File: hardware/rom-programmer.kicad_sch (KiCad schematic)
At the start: 4 parts, among them U1 74HC595, U2 74HC595, U3 28C256

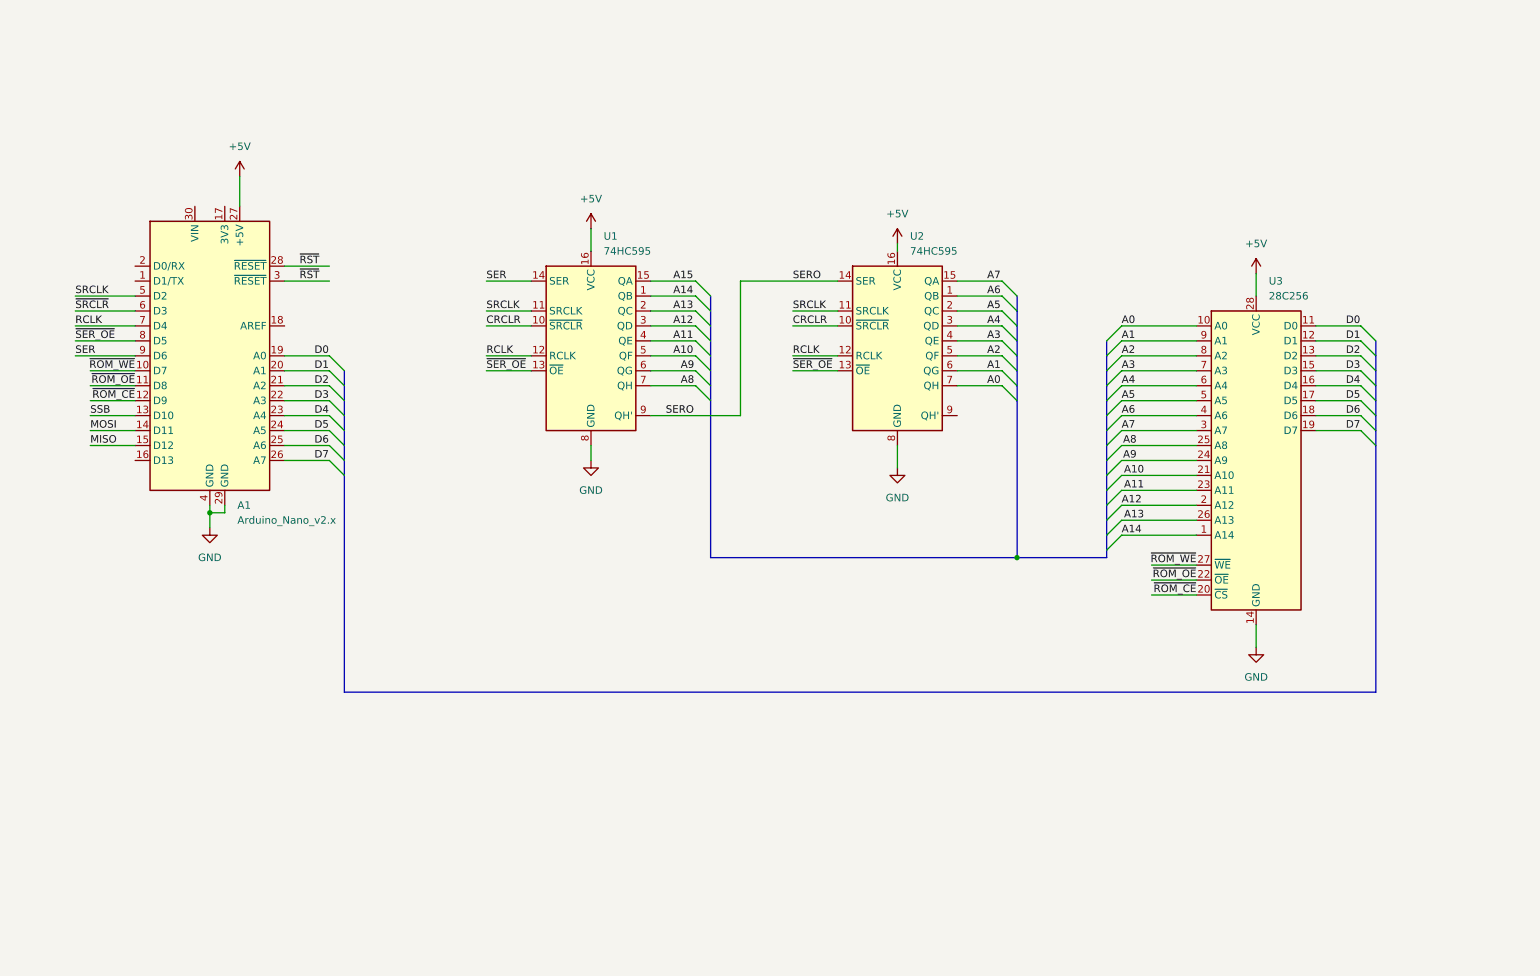
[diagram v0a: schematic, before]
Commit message: It can write bytes!
Co-authored-by: Copilot <copilot@github.com>
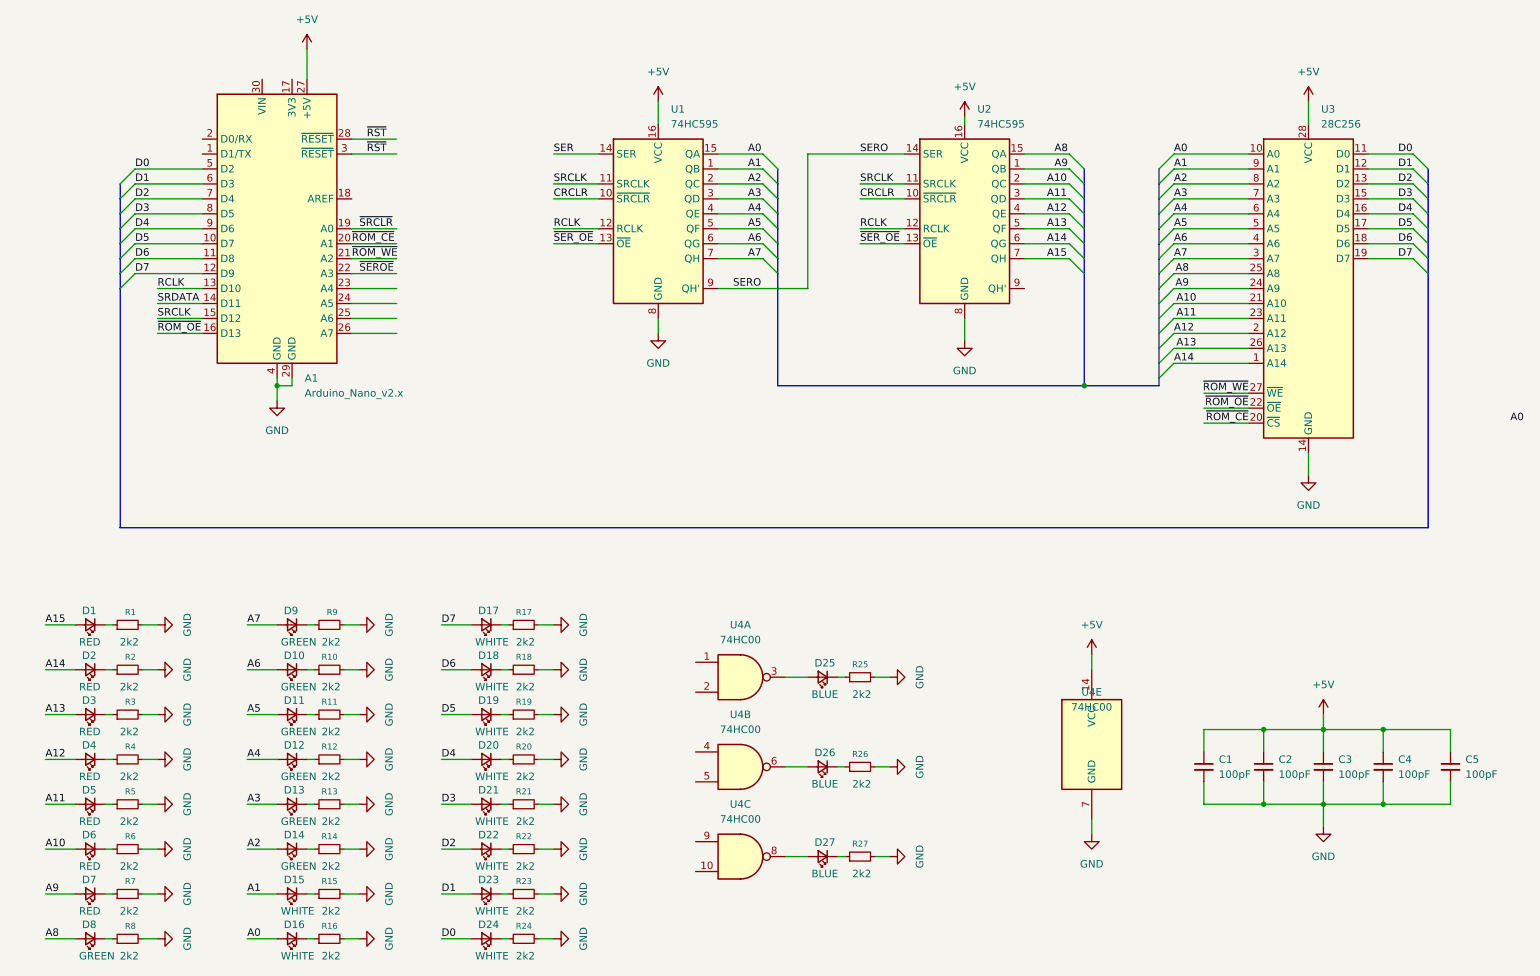
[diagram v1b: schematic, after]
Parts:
- added C1, C2, C3, C4, C5: 100pF, Capacitor_SMD:C_0805_2012Metric_Pad1.18x1.45mm_HandSolder, symbol Device:C_Small
- added D1, D2, D3, D4, D5, D6, D7: RED, Diode_SMD:D_0402_1005Metric_Pad0.77x0.64mm_HandSolder, symbol Device:LED_Small
- added D10, D11, D12, D13, D14, D8, D9: GREEN, Diode_SMD:D_0402_1005Metric_Pad0.77x0.64mm_HandSolder, symbol Device:LED_Small
- added D15, D16, D17, D18, D19, D20, D21, D22, D23, D24: WHITE, Diode_SMD:D_0402_1005Metric_Pad0.77x0.64mm_HandSolder, symbol Device:LED_Small
- added D25, D26, D27: BLUE, Diode_SMD:D_0402_1005Metric_Pad0.77x0.64mm_HandSolder, symbol Device:LED_Small
- added R1, R10, R11, R12, R13, R14, R15, R16, R17, R18, R19, R2, R20, R21, R22, R23, R24, R25, R26, R27, R3, R4, R5, R6, R7, R8, R9: 2k2, Resistor_SMD:R_0402_1005Metric_Pad0.72x0.64mm_HandSolder, symbol Device:R_Small
- added U4: 74HC00, Package_SO:SO-14_3.9x8.65mm_P1.27mm, symbol 74xx:74HC00
- U3: footprint (none) -> Socket:DIP_Socket-28_W11.9mm_W12.7mm_W15.24mm_W17.78mm_W18.5mm_3M_228-1277-00-0602J
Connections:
- net MISO is gone; now on net SRCLK: A1.15 (D12)
- net SSB is gone; now on net RCLK: A1.13 (D10)
- net +5V: now also C1.1, C2.1, C3.1, C4.1, C5.1, U4.14 (VCC)
- net A0: now also U1.15 (QA), D16.2 (A); no longer U2.7 (QH)
- net A1: now also U1.1 (QB), D15.2 (A); no longer U2.6 (QG)
- net A10: now also U2.2 (QC), D6.2 (A); no longer U1.5 (QF)
- net A11: now also U2.3 (QD), D5.2 (A); no longer U1.4 (QE)
- net A12: now also U2.4 (QE), D4.2 (A); no longer U1.3 (QD)
- net A13: now also U2.5 (QF), D3.2 (A); no longer U1.2 (QC)
- net A14: now also U2.6 (QG), D2.2 (A); no longer U1.1 (QB)
- net A15: now also U2.7 (QH), D1.2 (A); no longer U1.15 (QA)
- net A2: now also U1.2 (QC), D14.2 (A); no longer U2.5 (QF)
- net A3: now also U1.3 (QD), D13.2 (A); no longer U2.4 (QE)
- net A4: now also U1.4 (QE), D12.2 (A); no longer U2.3 (QD)
- net A5: now also U1.5 (QF), D11.2 (A); no longer U2.2 (QC)
- net A6: now also U1.6 (QG), D10.2 (A); no longer U2.1 (QB)
- net A7: now also U1.7 (QH), D9.2 (A); no longer U2.15 (QA)
- net A8: now also U2.15 (QA), D8.2 (A); no longer U1.7 (QH)
- net A9: now also U2.1 (QB), D7.2 (A); no longer U1.6 (QG)
- net D0: now also A1.5 (D2), D24.2 (A); no longer A1.19 (A0)
- net D1: now also A1.6 (D3), D23.2 (A); no longer A1.20 (A1)
- net D2: now also A1.7 (D4), D22.2 (A); no longer A1.21 (A2)
- net D3: now also A1.8 (D5), D21.2 (A); no longer A1.22 (A3)
- net D4: now also A1.9 (D6), D20.2 (A); no longer A1.23 (A4)
- net D5: now also A1.10 (D7), D19.2 (A); no longer A1.24 (A5)
- net D6: now also A1.11 (D8), D18.2 (A); no longer A1.25 (A6)
- net D7: now also A1.12 (D9), D17.2 (A); no longer A1.26 (A7)
- net GND: now also C1.2, C2.2, C3.2, C4.2, C5.2, R1.2, R10.2, R11.2, R12.2, R13.2, R14.2, R15.2, R16.2, R17.2, R18.2, R19.2, R2.2, R20.2, R21.2, R22.2, R23.2, R24.2, R25.2, R26.2, R27.2, R3.2, R4.2, R5.2, R6.2, R7.2, R8.2, R9.2, U4.7 (GND)
- net RCLK: no longer A1.7 (D4)
- net SER: no longer A1.9 (D6)
- net SRCLK: no longer A1.5 (D2)
- net ~{ROM_CE}: now also A1.20 (A1); no longer A1.12 (D9)
- net ~{ROM_OE}: now also A1.16 (D13); no longer A1.11 (D8)
- net ~{ROM_WE}: now also A1.21 (A2); no longer A1.10 (D7)
- net ~{SER_OE}: no longer A1.8 (D5)
- net ~{SRCLR}: now also A1.19 (A0); no longer A1.6 (D3)
- net MOSI renamed SRDATA
- new net: D26.2 (A), U4.6
- new net: D3.1 (K), R3.1
- new net: D16.1 (K), R16.1
- new net: D15.1 (K), R15.1
- new net: D26.1 (K), R26.1
- new net: D7.1 (K), R7.1
- new net: D14.1 (K), R14.1
- new net: D19.1 (K), R19.1
- new net: D8.1 (K), R8.1
- new net: D1.1 (K), R1.1
- new net: D4.1 (K), R4.1
- new net: D24.1 (K), R24.1
- new net: D11.1 (K), R11.1
- new net: D25.2 (A), U4.3
- new net: D21.1 (K), R21.1
- new net: D2.1 (K), R2.1
- new net: D13.1 (K), R13.1
- new net: D25.1 (K), R25.1
- new net: D20.1 (K), R20.1
- new net: D5.1 (K), R5.1
- new net: D18.1 (K), R18.1
- new net: D23.1 (K), R23.1
- new net: D17.1 (K), R17.1
- new net: D27.1 (K), R27.1
- new net: D27.2 (A), U4.8
- new net: D10.1 (K), R10.1
- new net: D9.1 (K), R9.1
- new net: D12.1 (K), R12.1
- new net: D22.1 (K), R22.1
- new net: D6.1 (K), R6.1
- new net ~{SEROE}: A1.22 (A3)
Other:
- moved on the sheet: A1, U1, U2, U3

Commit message: Erase and timing seems to work correctly and reliably now
Co-authored-by: Copilot <copilot@github.com>
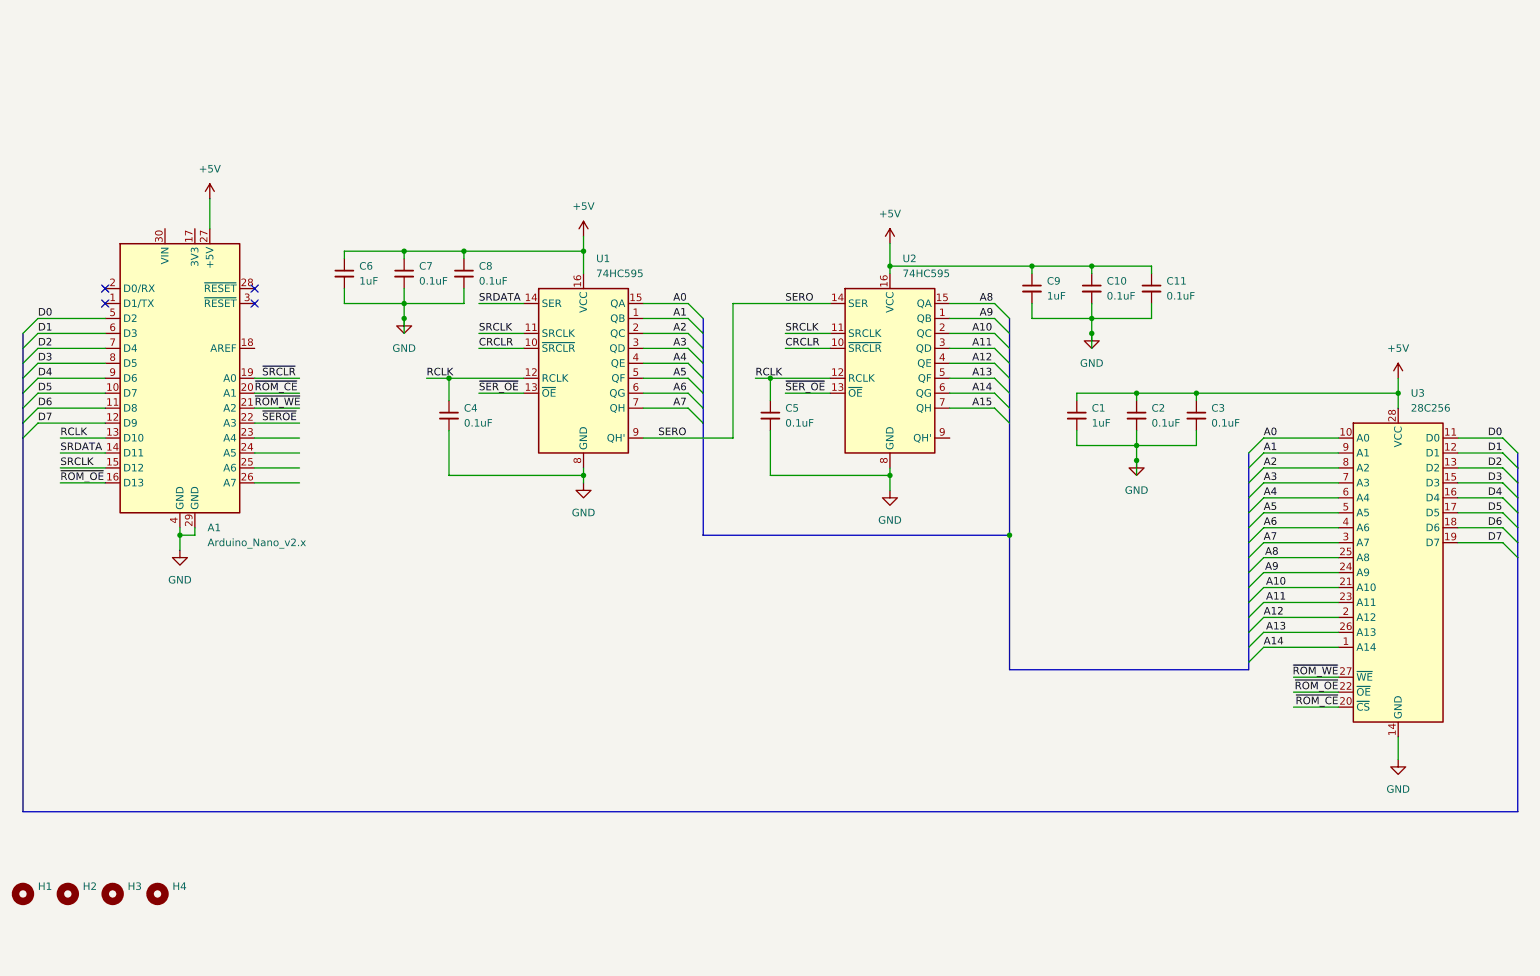
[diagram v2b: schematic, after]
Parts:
- removed D1, D2, D3, D4, D5, D6, D7: RED, Diode_SMD:D_0402_1005Metric_Pad0.77x0.64mm_HandSolder, symbol Device:LED_Small
- removed D10, D11, D12, D13, D14, D8, D9: GREEN, Diode_SMD:D_0402_1005Metric_Pad0.77x0.64mm_HandSolder, symbol Device:LED_Small
- removed D15, D16, D17, D18, D19, D20, D21, D22, D23, D24: WHITE, Diode_SMD:D_0402_1005Metric_Pad0.77x0.64mm_HandSolder, symbol Device:LED_Small
- removed D25, D26, D27: BLUE, Diode_SMD:D_0402_1005Metric_Pad0.77x0.64mm_HandSolder, symbol Device:LED_Small
- removed R1, R10, R11, R12, R13, R14, R15, R16, R17, R18, R19, R2, R20, R21, R22, R23, R24, R25, R26, R27, R3, R4, R5, R6, R7, R8, R9: 2k2, Resistor_SMD:R_0402_1005Metric_Pad0.72x0.64mm_HandSolder, symbol Device:R_Small
- removed U4: 74HC00, Package_SO:SO-14_3.9x8.65mm_P1.27mm, symbol 74xx:74HC00
- added C10, C11, C7, C8: 0.1uF, Capacitor_SMD:C_0402_1005Metric_Pad0.74x0.62mm_HandSolder, symbol Device:C_Small
- added C6, C9: 1uF, Capacitor_SMD:C_0805_2012Metric_Pad1.18x1.45mm_HandSolder, symbol Device:C_Small
- added H1, H2, H3, H4: MountingHole, MountingHole:MountingHole_2.2mm_M2, symbol Mechanical:MountingHole
- A1, U3: now left out of the parts list
- C1: value 100pF -> 1uF; Mouser SKU (none) -> 187-CL21B104KCFWPJF
- C2, C3, C4, C5: value 100pF -> 0.1uF; footprint Capacitor_SMD:C_0805_2012Metric_Pad1.18x1.45mm_HandSolder -> Capacitor_SMD:C_0402_1005Metric_Pad0.74x0.62mm_HandSolder; Mouser SKU (none) -> 187-CL05B104KO54PND
- U1, U2: Mouser SKU (none) -> 595-SN74HC595ANSR
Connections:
- net SER is gone; now on net SRDATA: U1.14 (SER)
- net +5V: now also C10.1, C11.1, C6.1, C7.1, C8.1, C9.1; no longer C4.1, C5.1
- net GND: now also C10.2, C11.2, C6.2, C7.2, C8.2, C9.2
- net RCLK: now also C4.1, C5.1
- net ~{RST}: no longer names the net of A1.28 (~{RESET})
- net ~{RST}: no longer A1.3 (~{RESET})
- no-connect marks 0 -> 4
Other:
- moved on the sheet: A1, U1, U2, U3
